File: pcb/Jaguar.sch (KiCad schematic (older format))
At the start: 39 parts, among them P1 12v-SW, P10 TPS, P11 Sensor-GND, P12 O2, P13 Sensor-GND, P14 CRANK+, P15 CRANK-, P16 CAM+, P17 CAM-, P18 DIS-BYPASS, P19 IGN-ADVANCE, P2 12v-SW2, P20 PT4-7, P21 INJ-IN, P22 INJ-GND, P25 FUEL-, P26 Injectors, P3 GND, P31 OUT-GND, P32 FUEL-12v, P33 Injectors-PB, P34 Injectors-IN, P35 FAN-, P36 FAN-12v, P37 ACC-, P38 ACC-12v, P39 FAN, P4 BRV-12v, P40 ACC, P41 MAF-Signal, P42 INJ-GND2, P43 Crank-Shield, P44 Cam-Shield, P45 Sensor-GND, P5 GND2, P6 IAT, P7 MAT, P8 COOLANT, P9 TPS-5v

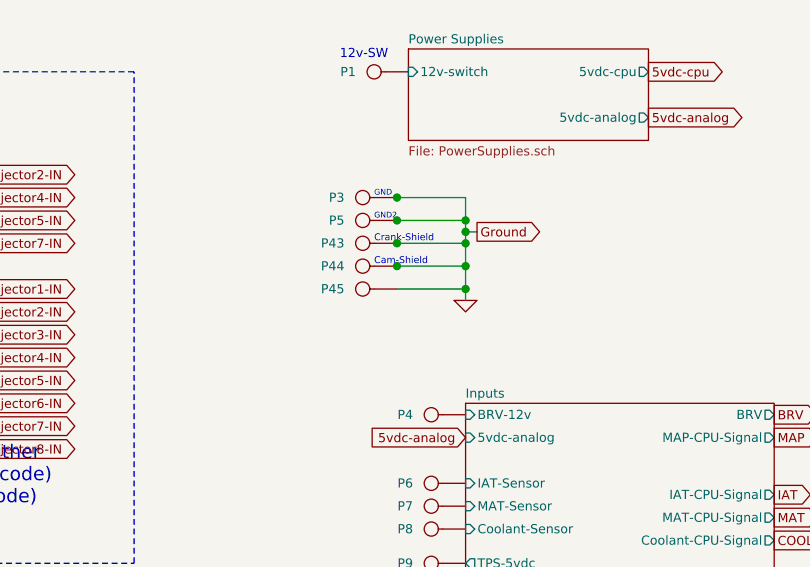
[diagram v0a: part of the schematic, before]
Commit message: Added Jaguar.lib to share KiCAD library, updated schematic files for this library
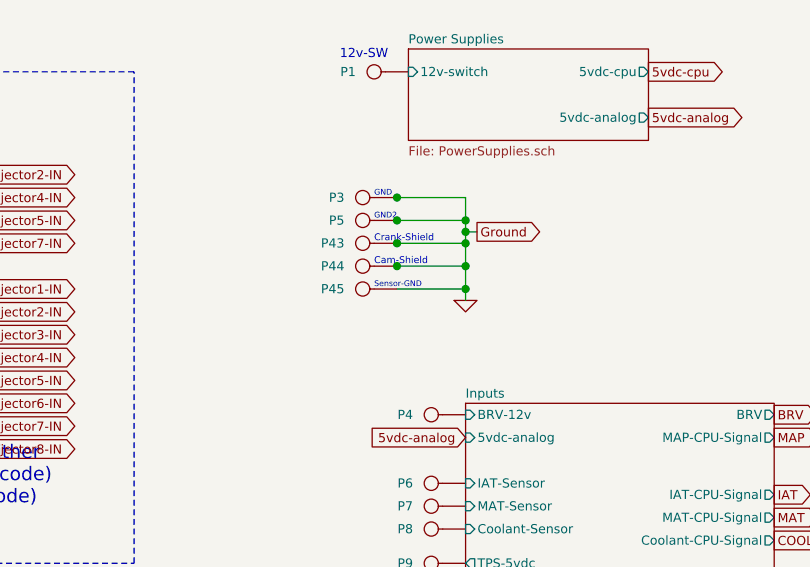
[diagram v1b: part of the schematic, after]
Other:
- note added: "Sensor-GND"
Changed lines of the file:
@@
-EESchema Schematic File Version 2  date Sun 05 Feb 2012 10:19:47 AM EST
+EESchema Schematic File Version 2  date Sun 05 Feb 2012 11:20:52 AM EST
 LIBS:power
 LIBS:device
@@
 LIBS:74xx
 LIBS:analog_switches
-LIBS:motorola
 LIBS:interface
 LIBS:opto
-LIBS:atmel
 LIBS:contrib
-LIBS:mc9s12xdp512
-LIBS:ft232rl
-LIBS:lm2937et
-LIBS:usb_b
-LIBS:freeEMS_lib
-LIBS:mpx4100a
+LIBS:Jaguar
 LIBS:Jaguar-cache
 EELAYER 24  0
@@
 Sheet 1 7
 Title "Jaguar PCB for FreeEMS"
-Date "4 feb 2012"
+Date "5 feb 2012"
 Rev "A.2"
 Comp "diyefi.org"
@@
 Comment4 ""
 $EndDescr
+Text Notes 8900 4350 0    25   ~ 0
+Sensor-GND
 Text Notes 8750 3350 0    40   ~ 0
 12v-SW

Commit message: Updated schematics, PDFs and PNGs with lumpensack2003 suggestions
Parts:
- P8: value COOLANT -> CHT
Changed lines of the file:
@@
-EESchema Schematic File Version 2  date Sun 05 Feb 2012 11:20:52 AM EST
+EESchema Schematic File Version 2  date Sun 05 Feb 2012 10:59:48 PM EST
+LIBS:opto
+LIBS:Jaguar
 LIBS:power
-LIBS:device
-LIBS:transistors
-LIBS:conn
-LIBS:linear
-LIBS:regul
-LIBS:74xx
-LIBS:analog_switches
-LIBS:interface
-LIBS:opto
-LIBS:contrib
-LIBS:Jaguar
 LIBS:Jaguar-cache
 EELAYER 24  0
@@
 Sheet 1 7
 Title "Jaguar PCB for FreeEMS"
-Date "5 feb 2012"
+Date "6 feb 2012"
 Rev "A.2"
 Comp "diyefi.org"
@@
 P 9150 5400
 F 0 "P8" H 9230 5400 40  0000 L CNN
-F 1 "COOLANT" H 9150 5455 30  0001 C CNN
+F 1 "CHT" H 9150 5455 30  0001 C CNN
 	1    9150 5400
 	-1   0    0    1

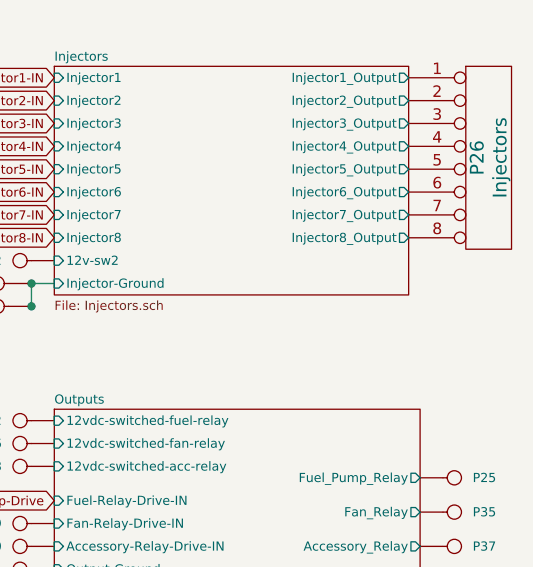
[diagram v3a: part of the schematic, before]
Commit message: Updated schematics for HCPL-061a Optocoupler
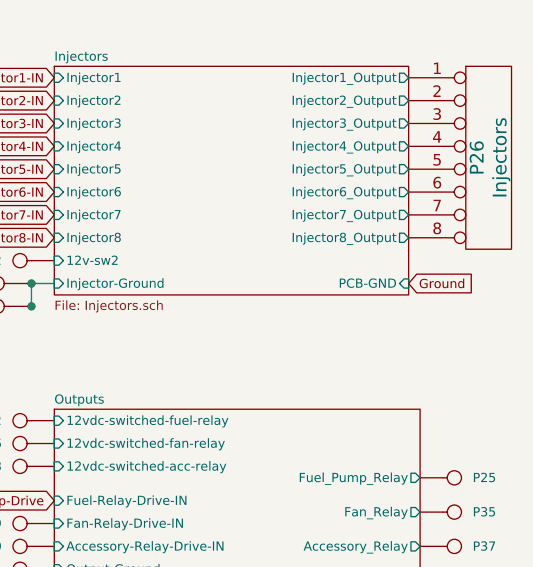
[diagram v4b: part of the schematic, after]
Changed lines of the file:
@@
-EESchema Schematic File Version 2  date Sat 18 Feb 2012 05:28:44 PM EST
+EESchema Schematic File Version 2  date Sun 19 Feb 2012 11:18:36 PM EST
 LIBS:opto
 LIBS:Jaguar
@@
 Sheet 1 7
 Title "Jaguar PCB for FreeEMS"
-Date "18 feb 2012"
+Date "20 feb 2012"
 Rev "A3"
 Comp "diyefi.org"
@@
 Comment4 ""
 $EndDescr
+Text GLabel 10600 1600 2    40   Input ~ 0
+Ground
 Text Notes 8900 4350 0    25   ~ 0
 Sensor-GND
@@
 F18 "Injector8" I L 9050 1400 40
 F19 "12v-sw2" I L 9050 1500 40
+F20 "PCB-GND" I R 10600 1600 40
 $EndSheet
 $Sheet

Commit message: Updated PDFs for Peer Review
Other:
- note added: "Jumpers labeled JP5 and JP6 are crossover wires,nothing \nmore. This was done to ease single sided PCB Prototype testing."
- note removed: "Jumpers labeled JP3, JP4, JP5 and JP6 are crossover wires,nothing \nmore. This was done to ease single sided PCB Prototype testing."
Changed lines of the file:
@@
-EESchema Schematic File Version 2  date Sun 19 Feb 2012 11:18:36 PM EST
+EESchema Schematic File Version 2  date 2/20/2012 12:13:35 AM
 LIBS:opto
 LIBS:Jaguar
@@
 LIBS:conn
 LIBS:Jaguar-cache
-EELAYER 24  0
+EELAYER 25  0
 EELAYER END
 $Descr A4 11700 8267
+encoding utf-8
 Sheet 1 7
 Title "Jaguar PCB for FreeEMS"
@@
 J2 is the TE Connectivity Automotive Grade water resistant connector. \nThe 35 positions will allow for modifications to the board for additional \ninputs/outputs as this design only uses 27 positions.  My samples to\ntest have arrived, http://www.te.com Part #'s:\n\n1-776163-2 Right Angle 35 Position Header (Natural Color)\nOR\n1-776231-2 Vertical 35 Position Header (Natural Color)\n1-776231-2 Vertical 35 Position Header (Natural Color)\n776164-2 35 Position AMP SEAL Plug Assembly (Natural Color)
 Text Notes 650  900  0    60   ~ 0
-Jumpers labeled JP3, JP4, JP5 and JP6 are crossover wires,nothing \nmore.  This was done to ease single sided PCB Prototype testing.
+Jumpers labeled JP5 and JP6 are crossover wires,nothing \nmore.  This was done to ease single sided PCB Prototype testing.
 Text Notes 600  700  0    70   ~ 14
 Notes:
